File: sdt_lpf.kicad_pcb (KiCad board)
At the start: 2 copper layers, 76.5 x 78.1 mm, 75 parts, among them J1 5-1814832-1, J2 5-1814832-1, J3 22-23-2021, J4 Conn_02x05_Odd_Even, U1 MASWSS0179, U10 MASWSS0179, U12 SN74HCS21, U13 74LVC1G04, U14 74LVC1G04, U15 74LVC1G04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

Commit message: Clean-up after first prototype build.
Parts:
- J4: footprint Connector_PinHeader_2.54mm:PinHeader_2x05_P2.54mm_Vertical -> Connector_IDC:IDC-Header_2x05_P2.54mm_Vertical
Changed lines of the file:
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@@
     )
   )
-  (footprint "Connector_PinHeader_2.54mm:PinHeader_2x05_P2.54mm_Vertical" (layer "F.Cu")
+  (footprint "Connector_IDC:IDC-Header_2x05_P2.54mm_Vertical" (layer "F.Cu")
     (at 103.42 115.58)
-    (descr "Through hole straight pin header, 2x05, 2.54mm pitch, double rows")
-    (tags "Through hole pin header THT 2x05 2.54mm double row")
+    (descr "Through hole IDC box header, 2x05, 2.54mm pitch, DIN 41651 / IEC 60603-13, double rows, https://docs.google.com/spreadsheets/d/16SsEcesNF15N3Lb4niX7dcUr-NY5_MFPQhobNuNppn4/edit#gid=0")
+    (tags "Through hole vertical IDC box header THT 2x05 2.54mm double row")
     (property "Sheetfile" "sdt_lpf.kicad_sch")
     (property "Sheetname" "")
@@
     (property "ki_keywords" "connector")
     (attr through_hole)
-    (fp_text reference "J4" (at 1.27 -2.33) (layer "F.SilkS")
+    (fp_text reference "J4" (at 1.27 -6.1) (layer "F.SilkS")
         (effects (font (size 1 1) (thickness 0.15)))
     )
-    (fp_text value "Conn_02x05_Odd_Even" (at 1.27 12.49) (layer "F.Fab")
+    (fp_text value "Conn_02x05_Odd_Even" (at 1.27 16.26) (layer "F.Fab")
         (effects (font (size 1 1) (thickness 0.15)))
     )
@@
         (effects (font (size 1 1) (thickness 0.15)))
     )
-    (fp_line (start -1.33 -1.33) (end 0 -1.33)
+    (fp_line (start -4.68 -0.5) (end -4.68 0.5)
       (stroke (width 0.12) (type solid)) (layer "F.SilkS"))
-    (fp_line (start -1.33 0) (end -1.33 -1.33)
+    (fp_line (start -4.68 0.5) (end -3.68 0)
       (stroke (width 0.12) (type solid)) (layer "F.SilkS"))
-    (fp_line (start -1.33 1.27) (end -1.33 11.49)
+    (fp_line (start -3.68 0) (end -4.68 -0.5)
       (stroke (width 0.12) (type solid)) (layer "F.SilkS"))
-    (fp_line (start -1.33 1.27) (end 1.27 1.27)
+    (fp_line (start -3.29 -5.21) (end 5.83 -5.21)
       (stroke (width 0.12) (type solid)) (layer "F.SilkS"))
-    (fp_line (start -1.33 11.49) (end 3.87 11.49)
+    (fp_line (start -3.29 3.03) (end -1.98 3.03)
       (stroke (width 0.12) (type solid)) (layer "F.SilkS"))
-    (fp_line (start 1.27 -1.33) (end 3.87 -1.33)
+    (fp_line (start -3.29 15.37) (end -3.29 -5.21)
       (stroke (width 0.12) (type solid)) (layer "F.SilkS"))
-    (fp_line (start 1.27 1.27) (end 1.27 -1.33)
+    (fp_line (start -1.98 -3.91) (end 4.52 -3.91)
       (stroke (width 0.12) (type solid)) (layer "F.SilkS"))
-    (fp_line (start 3.87 -1.33) (end 3.87 11.49)
+    (fp_line (start -1.98 3.03) (end -1.98 -3.91)
       (stroke (width 0.12) (type solid)) (layer "F.SilkS"))
-    (fp_line (start -1.8 -1.8) (end -1.8 11.95)
+    (fp_line (start -1.98 7.13) (end -3.29 7.13)
+      (stroke (width 0.12) (type solid)) (layer "F.SilkS"))
+    (fp_line (start -1.98 7.13) (end -1.98 7.13)
+      (stroke (width 0.12) (type solid)) (layer "F.SilkS"))
+    (fp_line (start -1.98 14.07) (end -1.98 7.13)
+      (stroke (width 0.12) (type solid)) (layer "F.SilkS"))
+    (fp_line (start 4.52 -3.91) (end 4.52 14.07)
+      (stroke (width 0.12) (type solid)) (layer "F.SilkS"))
+    (fp_line (start 4.52 14.07) (end -1.98 14.07)
+      (stroke (width 0.12) (type solid)) (layer "F.SilkS"))
+    (fp_line (start 5.83 -5.21) (end 5.83 15.37)
+      (stroke (width 0.12) (type solid)) (layer "F.SilkS"))
+    (fp_line (start 5.83 15.37) (end -3.29 15.37)
+      (stroke (width 0.12) (type solid)) (layer "F.SilkS"))
+    (fp_line (start -3.68 -5.6) (end -3.68 15.76)
       (stroke (width 0.05) (type solid)) (layer "F.CrtYd"))
-    (fp_line (start -1.8 11.95) (end 4.35 11.95)
+    (fp_line (start -3.68 15.76) (end 6.22 15.76)
       (stroke (width 0.05) (type solid)) (layer "F.CrtYd"))
-    (fp_line (start 4.35 -1.8) (end -1.8 -1.8)
+    (fp_line (start 6.22 -5.6) (end -3.68 -5.6)
       (stroke (width 0.05) (type solid)) (layer "F.CrtYd"))
-    (fp_line (start 4.35 11.95) (end 4.35 -1.8)
+    (fp_line (start 6.22 15.76) (end 6.22 -5.6)
       (stroke (width 0.05) (type solid)) (layer "F.CrtYd"))
-    (fp_line (start -1.27 0) (end 0 -1.27)
+    (fp_line (start -3.18 -4.1) (end -2.18 -5.1)
       (stroke (width 0.1) (type solid)) (layer "F.Fab"))
-    (fp_line (start -1.27 11.43) (end -1.27 0)
+    (fp_line (start -3.18 3.03) (end -1.98 3.03)
       (stroke (width 0.1) (type solid)) (layer "F.Fab"))
-    (fp_line (start 0 -1.27) (end 3.81 -1.27)
+    (fp_line (start -3.18 15.26) (end -3.18 -4.1)
       (stroke (width 0.1) (type solid)) (layer "F.Fab"))
-    (fp_line (start 3.81 -1.27) (end 3.81 11.43)
+    (fp_line (start -2.18 -5.1) (end 5.72 -5.1)
       (stroke (width 0.1) (type solid)) (layer "F.Fab"))
-    (fp_line (start 3.81 11.43) (end -1.27 11.43)
+    (fp_line (start -1.98 -3.91) (end 4.52 -3.91)
       (stroke (width 0.1) (type solid)) (layer "F.Fab"))
-    (pad "1" thru_hole rect (at 0 0) (size 1.7 1.7) (drill 1) (layers "*.Cu" "*.Mask")
+    (fp_line (start -1.98 3.03) (end -1.98 -3.91)
+      (stroke (width 0.1) (type solid)) (layer "F.Fab"))
+    (fp_line (start -1.98 7.13) (end -3.18 7.13)
+      (stroke (width 0.1) (type solid)) (layer "F.Fab"))
+    (fp_line (start -1.98 7.13) (end -1.98 7.13)
+      (stroke (width 0.1) (type solid)) (layer "F.Fab"))
+    (fp_line (start -1.98 14.07) (end -1.98 7.13)
+      (stroke (width 0.1) (type solid)) (layer "F.Fab"))
+    (fp_line (start 4.52 -3.91) (end 4.52 14.07)
+      (stroke (width 0.1) (type solid)) (layer "F.Fab"))
+    (fp_line (start 4.52 14.07) (end -1.98 14.07)
+      (stroke (width 0.1) (type solid)) (layer "F.Fab"))
+    (fp_line (start 5.72 -5.1) (end 5.72 15.26)
+      (stroke (width 0.1) (type solid)) (layer "F.Fab"))
+    (fp_line (start 5.72 15.26) (end -3.18 15.26)
+      (stroke (width 0.1) (type solid)) (layer "F.Fab"))
+    (pad "1" thru_hole roundrect (at 0 0) (size 1.7 1.7) (drill 1) (layers "*.Cu" "*.Mask") (roundrect_rratio 0.147059)
       (net 30 "/80M_ON") (pinfunction "Pin_1") (pintype "passive"))
-    (pad "2" thru_hole oval (at 2.54 0) (size 1.7 1.7) (drill 1) (layers "*.Cu" "*.Mask")
+    (pad "2" thru_hole circle (at 2.54 0) (size 1.7 1.7) (drill 1) (layers "*.Cu" "*.Mask")
       (net 31 "/40M_ON") (pinfunction "Pin_2") (pintype "passive"))
-    (pad "3" thru_hole oval (at 0 2.54) (size 1.7 1.7) (drill 1) (layers "*.Cu" "*.Mask")
+    (pad "3" thru_hole circle (at 0 2.54) (size 1.7 1.7) (drill 1) (layers "*.Cu" "*.Mask")
       (net 32 "/20M_ON") (pinfunction "Pin_3") (pintype "passive"))
-    (pad "4" thru_hole oval (at 2.54 2.54) (size 1.7 1.7) (drill 1) (layers "*.Cu" "*.Mask")
+    (pad "4" thru_hole circle (at 2.54 2.54) (size 1.7 1.7) (drill 1) (layers "*.Cu" "*.Mask")
       (net 38 "/15M_ON") (pinfunction "Pin_4") (pintype "passive"))
-    (pad "5" thru_hole oval (at 0 5.08) (size 1.7 1.7) (drill 1) (layers "*.Cu" "*.Mask")
+    (pad "5" thru_hole circle (at 0 5.08) (size 1.7 1.7) (drill 1) (layers "*.Cu" "*.Mask")
       (net 51 "unconnected-(J4-Pin_5-Pad5)") (pinfunction "Pin_5") (pintype "passive+no_connect"))
-    (pad "6" thru_hole oval (at 2.54 5.08) (size 1.7 1.7) (drill 1) (layers "*.Cu" "*.Mask")
+    (pad "6" thru_hole circle (at 2.54 5.08) (size 1.7 1.7) (drill 1) (layers "*.Cu" "*.Mask")
       (net 52 "unconnected-(J4-Pin_6-Pad6)") (pinfunction "Pin_6") (pintype "passive+no_connect"))
-    (pad "7" thru_hole oval (at 0 7.62) (size 1.7 1.7) (drill 1) (layers "*.Cu" "*.Mask")
+    (pad "7" thru_hole circle (at 0 7.62) (size 1.7 1.7) (drill 1) (layers "*.Cu" "*.Mask")
       (net 53 "unconnected-(J4-Pin_7-Pad7)") (pinfunction "Pin_7") (pintype "passive+no_connect"))
-    (pad "8" thru_hole oval (at 2.54 7.62) (size 1.7 1.7) (drill 1) (layers "*.Cu" "*.Mask")
+    (pad "8" thru_hole circle (at 2.54 7.62) (size 1.7 1.7) (drill 1) (layers "*.Cu" "*.Mask")
       (net 50 "/3_3V") (pinfunction "Pin_8") (pintype "passive"))
-    (pad "9" thru_hole oval (at 0 10.16) (size 1.7 1.7) (drill 1) (layers "*.Cu" "*.Mask")
+    (pad "9" thru_hole circle (at 0 10.16) (size 1.7 1.7) (drill 1) (layers "*.Cu" "*.Mask")
       (net 8 "GND") (pinfunction "Pin_9") (pintype "passive"))
-    (pad "10" thru_hole oval (at 2.54 10.16) (size 1.7 1.7) (drill 1) (layers "*.Cu" "*.Mask")
+    (pad "10" thru_hole circle (at 2.54 10.16) (size 1.7 1.7) (drill 1) (layers "*.Cu" "*.Mask")
       (net 34 "/RXTX") (pinfunction "Pin_10") (pintype "passive"))
-    (model "${KICAD6_3DMODEL_DIR}/Connector_PinHeader_2.54mm.3dshapes/PinHeader_2x05_P2.54mm_Vertical.wrl"
+    (model "${KICAD6_3DMODEL_DIR}/Connector_IDC.3dshapes/IDC-Header_2x05_P2.54mm_Vertical.wrl"
       (offset (xyz 0 0 0))
       (scale (xyz 1 1 1))

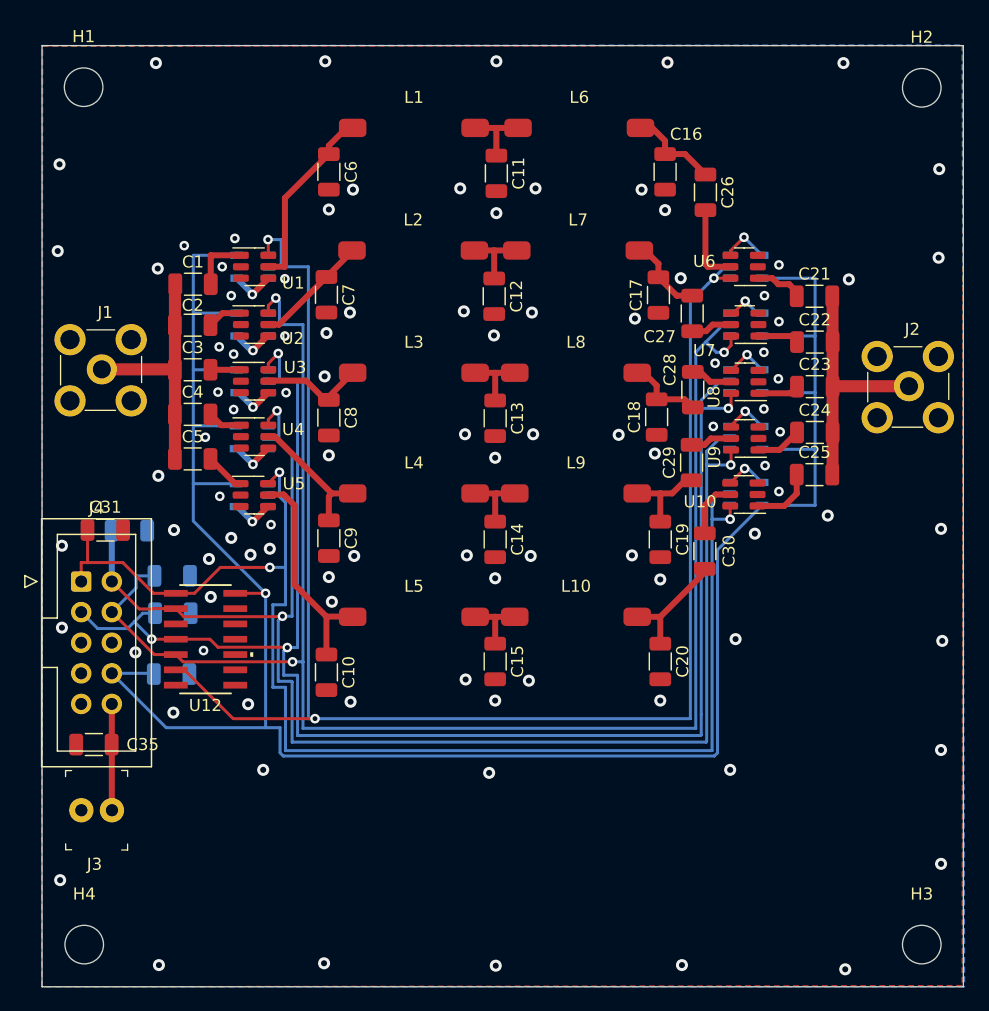
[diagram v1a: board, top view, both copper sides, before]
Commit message: Fixed logic gate, is now NOR.  Cleaned up layout.
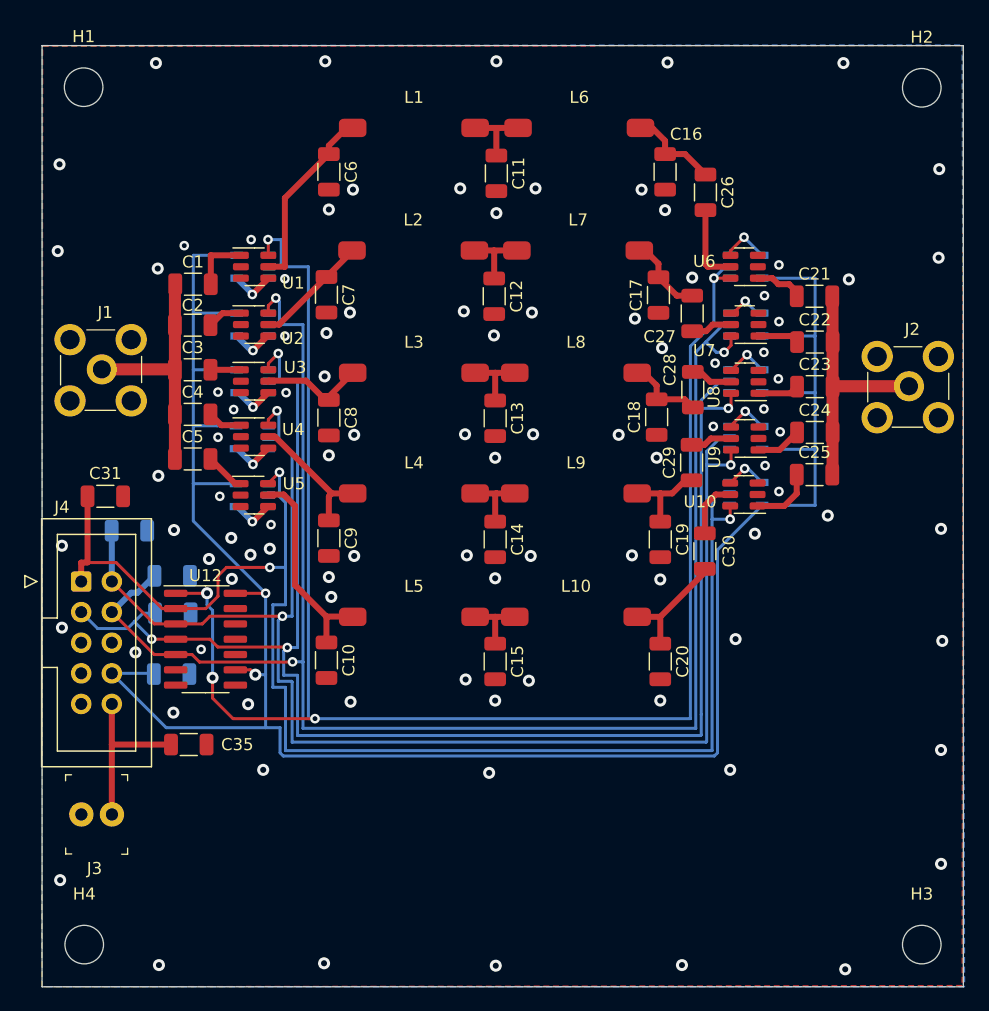
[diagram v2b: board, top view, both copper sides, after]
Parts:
- U12: value SN74HCS21 -> 4002; footprint 74LVC14:SO14_DIO -> Package_SO:SOIC-14_3.9x8.7mm_P1.27mm
- moved C35 7.88 mm to (112.3, 129.1), turned to 180 degrees
- moved C31 2.80 mm to (105.4, 108.5)
- moved C10 1.00 mm to (123.8, 122.1)
- moved J3 0.35 mm to (106.0, 134.9)
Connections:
- U12 pad 1: /80M_ON -> /10M_ON
- U12 pad 11: unconnected-(U12-NC-Pad11) -> GND
- U12 pad 13: GND -> unconnected-(U12-Pad13)
- U12 pad 2: /40M_ON -> /80M_ON
- U12 pad 3: unconnected-(U12-NC-Pad3) -> /40M_ON
- U12 pad 6: /10M_ON -> (no net)
- U12 pad 8: unconnected-(U12-2Y-Pad8) -> (no net)
- U12 pad 9: GND -> /3_3V
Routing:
- net /10M_ON: track 130.9 -> 138.7 mm, vias 3 -> 5
- net /RXTX: track 8.82 -> 14.1 mm
- net /80M_ON: track 111.4 -> 116.2 mm
- net /3_3V: track 183.0 -> 185.6 mm, vias 1 -> 2
- net Net-(U5-RFC): track 18.2 -> 17.2 mm
- net /15M_ON: track 134.1 -> 133.6 mm
- net /40M_ON: track 116.2 -> 116.7 mm
- net GND: vias 99 -> 97

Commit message: Mostly completed clean-up.
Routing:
- net /20M_ON: track 127.4 -> 126.1 mm
- net /15M_ON: track 133.6 -> 132.7 mm
- net /10M_ON: track 138.7 -> 138.0 mm
- net /40M_ON: track 116.7 -> 117.3 mm
- net /80M_ON: track 116.2 -> 116.7 mm
- net GND: vias 97 -> 98
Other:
- board text added: "KF5N"
- board text added: "T41 EXPERIMENTAL PLATFORM"

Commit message: Ready to release to fab.
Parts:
- C35: moved to B.Cu
- moved C35 4.90 mm to (107.4, 129.3)
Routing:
- net /3_3V: track 185.6 -> 184.1 mm
- net /RXTX: track 14.1 -> 12.7 mm
- net GND: vias 98 -> 104
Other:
- board text added: "5 BAND LOW PASS FILTER"
